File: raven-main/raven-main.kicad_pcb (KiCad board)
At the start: 4 copper layers, 76 parts, among them J1 RBUS, J2 USB_C_Receptacle_USB2.0, U1 ESP32-S3, U2 SN65HVD230, U3 LM66200DRLR, U4 MAX77827AEFD+T, U5 SC4215ASTRT, Y1 R940000171

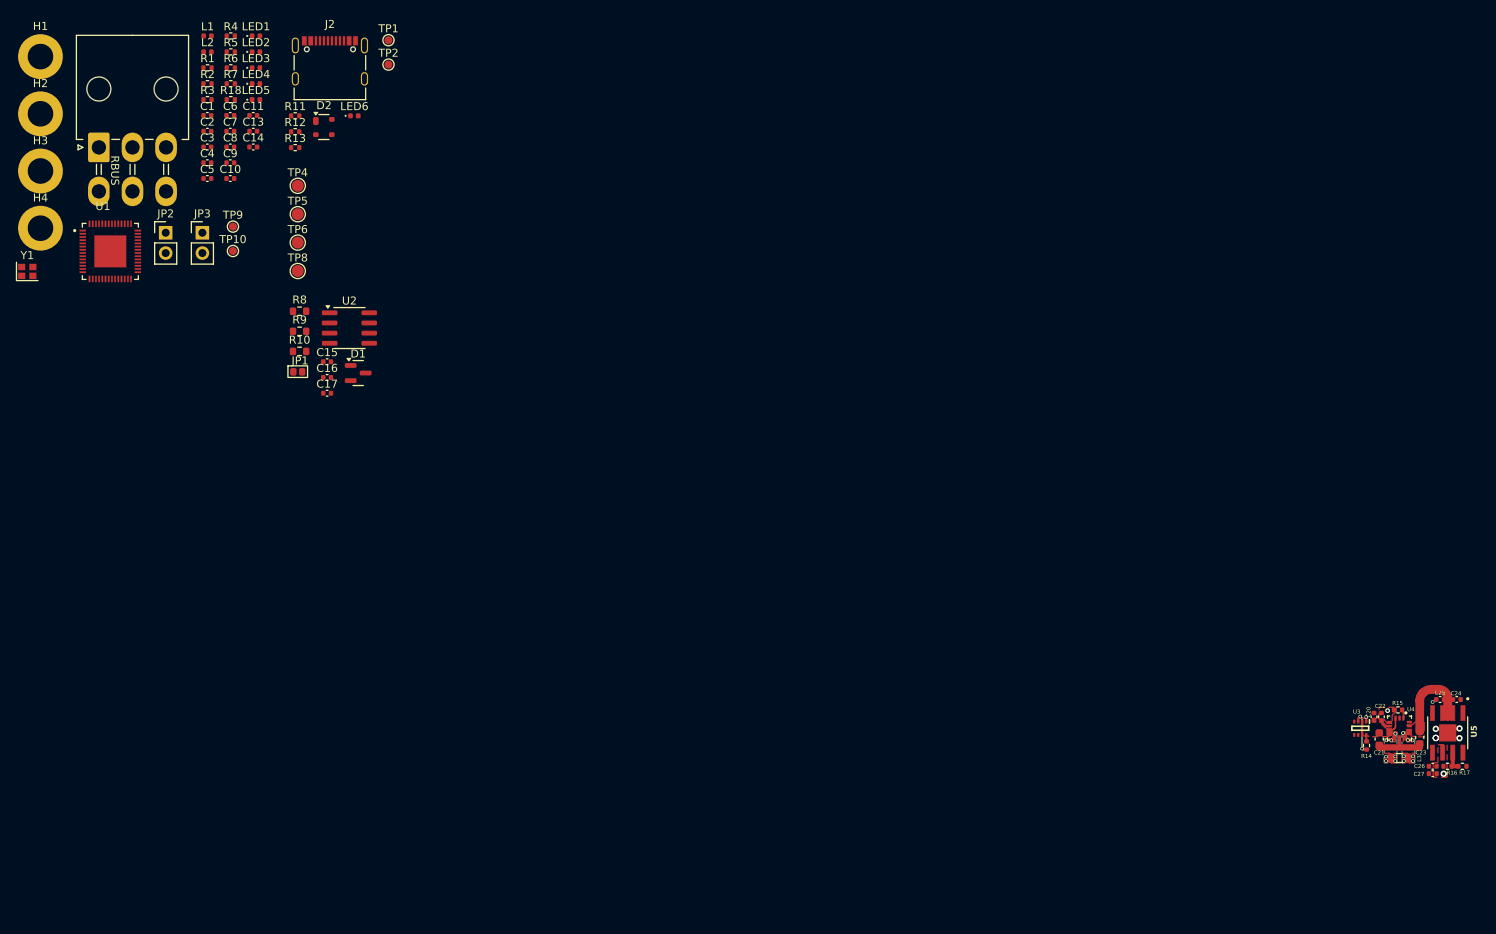
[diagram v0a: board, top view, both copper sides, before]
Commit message: Added missing footprints
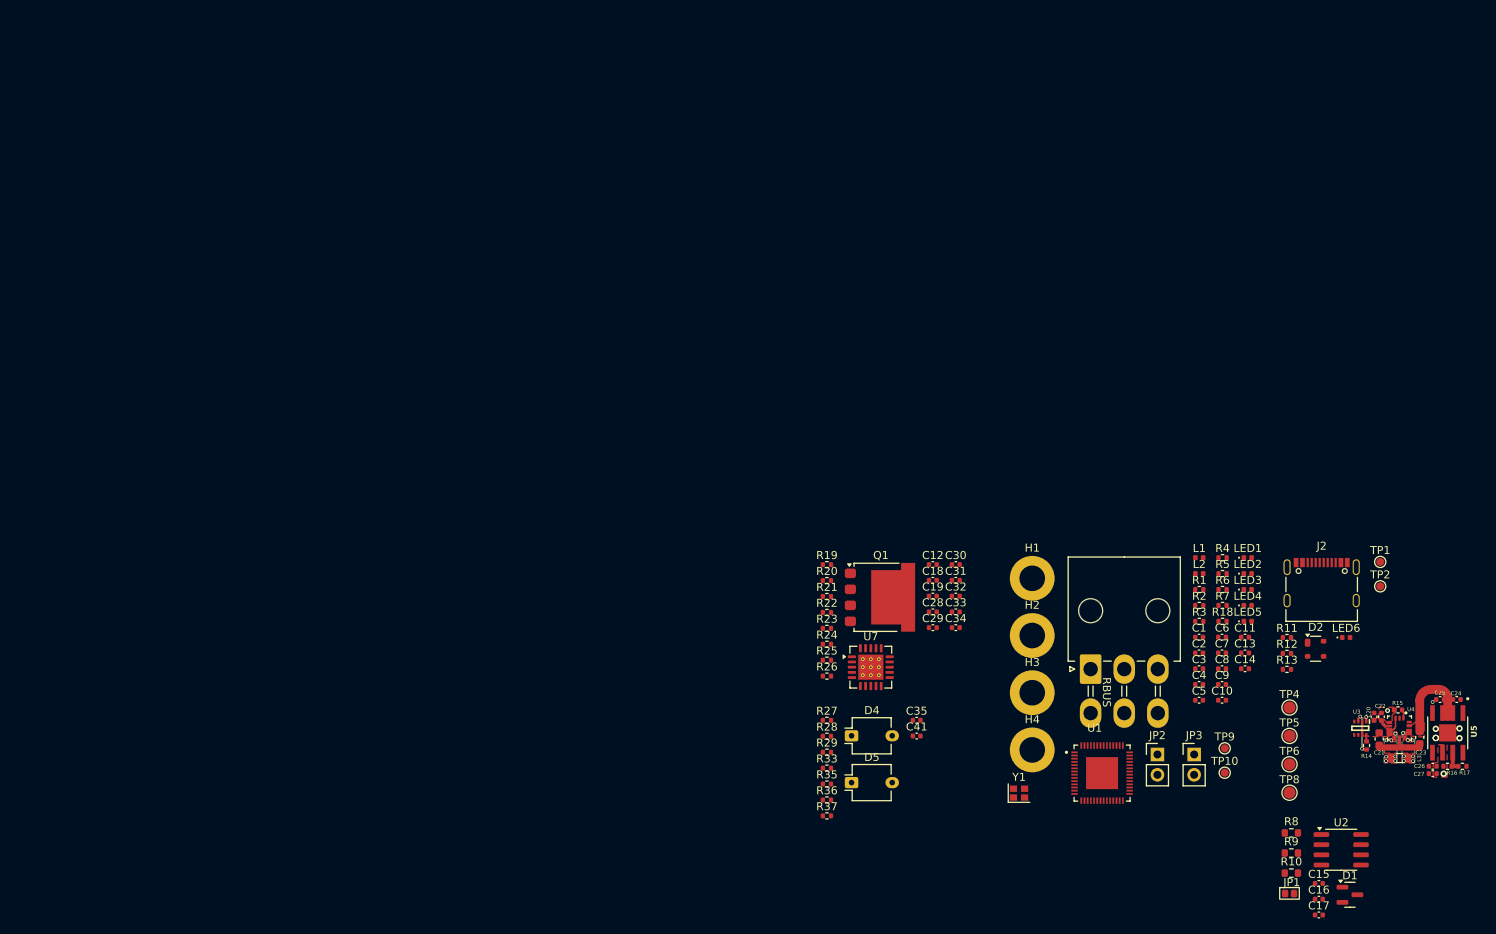
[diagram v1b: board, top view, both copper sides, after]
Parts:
- added C12: 6.8nF, Capacitor_SMD:C_0402_1005Metric, F.Cu at (114.6, 66.6)
- added C18: 68uF, Capacitor_SMD:C_0402_1005Metric, F.Cu at (114.6, 68.5)
- added C19: 68pF, Capacitor_SMD:C_0402_1005Metric, F.Cu at (114.6, 70.5)
- added C28: 10uF, Capacitor_SMD:C_0402_1005Metric, F.Cu at (114.6, 72.5)
- added C29: 2.2uF, Capacitor_SMD:C_0402_1005Metric, F.Cu at (114.6, 74.5)
- added C30: 1uF, Capacitor_SMD:C_0402_1005Metric, F.Cu at (117.5, 66.6)
- added C31: 47uF, Capacitor_SMD:C_0402_1005Metric, F.Cu at (117.5, 68.5)
- added C32: 100nF, Capacitor_SMD:C_0402_1005Metric, F.Cu at (117.5, 70.5)
- added C33: 22pF, Capacitor_SMD:C_0402_1005Metric, F.Cu at (117.5, 72.5)
- added C34: 100nF, Capacitor_SMD:C_0402_1005Metric, F.Cu at (117.5, 74.5)
- added C35: 0.5pF, Capacitor_SMD:C_0402_1005Metric, F.Cu at (112.6, 86.0)
- added C41: 0.5pF, Capacitor_SMD:C_0402_1005Metric, F.Cu at (112.6, 88.0)
- added D4: BPW34, OptoDevice:Osram_DIL2_4.3x4.65mm_P5.08mm, F.Cu at (104.5, 88.0)
- added D5: BPW34, OptoDevice:Osram_DIL2_4.3x4.65mm_P5.08mm, F.Cu at (104.5, 93.8)
- added Q1: SQJQ100EL, Package_TO_SOT_SMD:LFPAK88, F.Cu at (108.1, 70.7)
- added R19: 2.05k, Resistor_SMD:R_0402_1005Metric, F.Cu at (101.4, 66.6)
- added R20: 10k, Resistor_SMD:R_0402_1005Metric, F.Cu at (101.4, 68.6)
- added R21: 25.5k, Resistor_SMD:R_0402_1005Metric, F.Cu at (101.4, 70.6)
- added R22: 10k, Resistor_SMD:R_0402_1005Metric, F.Cu at (101.4, 72.6)
- added R23: 10.7k, Resistor_SMD:R_0402_1005Metric, F.Cu at (101.4, 74.5)
- added R24: 100, Resistor_SMD:R_0402_1005Metric, F.Cu at (101.4, 76.5)
- added R25: 20m, Resistor_SMD:R_0402_1005Metric, F.Cu at (101.4, 78.5)
- added R26: 100, Resistor_SMD:R_0402_1005Metric, F.Cu at (101.4, 80.5)
- added R27: 1G, Resistor_SMD:R_0402_1005Metric, F.Cu at (101.4, 86.0)
- added R28: 100k, Resistor_SMD:R_0402_1005Metric, F.Cu at (101.4, 88.0)
- added R29: R_Variable, Resistor_SMD:R_0402_1005Metric, F.Cu at (101.4, 90.0)
- added R33: 1G, Resistor_SMD:R_0402_1005Metric, F.Cu at (101.4, 92.0)
- added R35: 100k, Resistor_SMD:R_0402_1005Metric, F.Cu at (101.4, 94.0)
- added R36: R_Variable, Resistor_SMD:R_0402_1005Metric, F.Cu at (101.4, 96.0)
- added R37: 200, Resistor_SMD:R_0402_1005Metric, F.Cu at (101.4, 98.0)
- added U7: TPS7A4701xRGW, Package_DFN_QFN:Texas_RGW0020A_VQFN-20-1EP_5x5mm_P0.65mm_EP3.15x3.15mm_ThermalVias, F.Cu at (106.9, 79.4)
- moved C1 140.1 mm to (147.9, 75.7)
- moved C10 140.1 mm to (150.8, 83.5)
- moved C11 140.1 mm to (153.6, 75.7)
- moved C13 140.1 mm to (153.6, 77.6)
- moved C14 140.1 mm to (153.6, 79.6)
- moved C15 140.1 mm to (162.9, 106.4)
- moved C16 140.1 mm to (162.9, 108.4)
- moved C17 140.1 mm to (162.9, 110.4)
- moved C2 140.1 mm to (147.9, 77.6)
- moved C3 140.1 mm to (147.9, 79.6)
- moved C4 140.1 mm to (147.9, 81.6)
- moved C5 140.1 mm to (147.9, 83.5)
- moved C6 140.1 mm to (150.8, 75.7)
- moved C7 140.1 mm to (150.8, 77.6)
- moved C8 140.1 mm to (150.8, 79.6)
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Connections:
- C1 pad 2: GND -> +50V
- C10 pad 2: GND -> +50V
- C11 pad 2: GND -> +50V
- C13 pad 2: GND -> +50V
- C14 pad 2: GND -> +50V
- C15 pad 2: GND -> +50V
- C16 pad 2: GND -> +50V
- C17 pad 2: GND -> +50V
- C2 pad 2: GND -> +50V
- C20 pad 1: /Power/BBIN -> +50V
- C20 pad 2: GND -> +50V
- C21 pad 1: /Power/BBIN -> +50V
- C21 pad 2: GND -> +50V
- C22 pad 2: GND -> +50V
- C23 pad 2: GND -> +50V
- C24 pad 2: GND -> +50V
- C25 pad 2: GND -> +50V
- C26 pad 1: GND -> +50V
- C27 pad 1: GND -> +50V
- C3 pad 2: GND -> +50V
- C4 pad 2: GND -> +50V
- C5 pad 2: GND -> +50V
- C6 pad 2: GND -> +50V
- C7 pad 2: GND -> +50V
- C8 pad 2: GND -> +50V
- C9 pad 2: GND -> +50V
- D1 pad 3: GND -> +50V
- D2 pad 1: GND -> +50V
- H1 pad 1: GND -> +50V
- H2 pad 1: GND -> +50V
- H3 pad 1: GND -> +50V
- H4 pad 1: GND -> +50V
- J1 pad 1: GND -> +50V
- J1 pad 2: GND -> +50V
- J2 pad A1: GND -> +50V
- J2 pad A12: GND -> +50V
- J2 pad B1: GND -> +50V
- J2 pad B12: GND -> +50V
- J2 pad S1: GND -> +50V
- JP2 pad 2: GND -> +50V
- JP3 pad 2: GND -> +50V
- LED4 pad 1: GND -> +50V
- LED5 pad 1: GND -> +50V
- LED6 pad 1: GND -> +50V
- R11 pad 2: GND -> +50V
- R12 pad 1: GND -> +50V
- R15 pad 2: GND -> +50V
- R17 pad 2: GND -> +50V
- R8 pad 2: GND -> +50V
- TP4 pad 1: /Power/BBIN -> +50V
- U1 pad 57: GND -> +50V
- U1 pad 6: unconnected-(U1-GPIO1/ADC1_CH0-Pad6) -> /Detector_Out_A
- U1 pad 7: unconnected-(U1-GPIO2/ADC1_CH1-Pad7) -> /Detector_Out_B
- U2 pad 2: GND -> +50V
- U3 pad 1: GND -> +50V
- U3 pad 2: /Power/BBIN -> +50V
- U3 pad 4: GND -> +50V
- U3 pad 5: GND -> +50V
- U3 pad 7: /Power/BBIN -> +50V
- U4 pad 3: /Power/BBIN -> +50V
- U4 pad 4: GND -> +50V
- U4 pad 6: /Power/BBIN -> +50V
- U4 pad 9: GND -> +50V
- U5 pad 8: GND -> +50V
- U5 pad 9: GND -> +50V
- Y1 pad 2: GND -> +50V
- Y1 pad 4: GND -> +50V
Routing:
- net +50V: track 0.00 -> 11.0 mm, vias 0 -> 8
- net GND: track 7.31 -> 0.00 mm, vias 8 -> 0
- net /Power/BBIN: track 3.68 -> 0.00 mm
- added copper zone on F.Cu, net +50V
- removed copper zone on F.Cu, net /Power/BBIN
- removed copper zone on F.Cu, net GND
